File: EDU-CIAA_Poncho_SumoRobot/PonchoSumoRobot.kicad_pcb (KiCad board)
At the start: 2 copper layers, 49 parts, among them K1 RELAY_C, K2 RELAY_C, K3 RELAY_C, K4 RELAY_C, P1 CONN_01X02, P11 CONN_01X02, P12 CONN_01X02, P13 CONN_01X02, P14 CONN_01X02, P15 CONN_01X02, P16 CONN_01X02, P17 CONN_01X02, P18 CONN_01X02, P2 CONN_01X04, P3 CONN_02X09, P4 CONN_01X02, P5 CONN_01X02, P6 CONN_01X04, Q1 BC817-40, Q2 BC817-40, Q3 BC817-40, Q4 BC817-40, U5 40106

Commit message: Reorganizo bibliotecas en esquemático y PCB. Reparo señal de 12V. Agrego Footprints. Coloco plantilla EDU-CIAA. Reparo asociación conector EDU-CIAA en sch y pcb.
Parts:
- removed XA2: Conn_PonchoMP_2x_20x2, Poncho_Esqueleto:Conn_Poncho_Completo
- added G***: LOGO, sumo_robot:Logo_Poncho, F.Cu at (158.8, 137.2)
- added G***: Logo_EDU-CIAA, sumo_robot:Logo_EDU-CIAA, F.Cu at (160.0, 154.9)
- added G101: Logo_OSHWA, sumo_robot:Logo_OSHWA, F.Cu at (158.8, 125.7)
- added MP?: Plantilla_EDU-CIAA, sumo_robot:Plantilla_EDU-CIAA, F.Cu at (119.4, 92.7)
- D1, D2, D3, D4: footprint LEDs:LED_1206 -> sumo_robot:LED_1206
- D5, D6, D7, D8: footprint Diodes_ThroughHole:Diode_DO-41_SOD81_Horizontal_RM10 -> sumo_robot:Diode_DO-41_SOD81_Horizontal_RM10
- K1, K2, K3, K4: footprint Relays_ThroughHole:Relay_SANYOU_SRD_Series_Form_C -> sumo_robot:Relay_SANYOU_SRD_Series_Form_C
- P1, P4, P5: footprint Connect:bornier2 -> sumo_robot:bornier2
- P11, P12, P13, P14, P15, P16, P17, P18: footprint Pin_Headers:Pin_Header_Straight_1x02 -> sumo_robot:Pin_Header_Straight_1x02
- P2, P6: footprint Pin_Headers:Pin_Header_Straight_1x04 -> sumo_robot:Pin_Header_Straight_1x04
- P3: footprint Pin_Headers:Pin_Header_Straight_2x09 -> sumo_robot:Pin_Header_Straight_2x09
- Q1, Q2, Q3, Q4: footprint TO_SOT_Packages_SMD:SOT-23 -> sumo_robot:SOT-23
- R10, R11, R12, R13, R14, R15, R16, R17, R18, R19, R20, R5, R6, R7, R8, R9: footprint Resistors_ThroughHole:Resistor_Horizontal_RM7mm -> sumo_robot:Resistor_Horizontal_RM7mm
- U5: footprint 40xx:40xx-DIL14 -> sumo_robot:40xx-DIL14
- XA1: footprint Poncho_Esqueleto:Conn_Poncho_Completo -> sumo_robot:Conn_Poncho_SinBorde
- moved XA1 126.4 mm to (119.4, 92.7)
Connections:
- K1 pad 3: Net-(K1-Pad3) -> +12V
- K2 pad 3: Net-(K2-Pad3) -> +12V
- K3 pad 3: Net-(K3-Pad3) -> +12V
- K4 pad 3: Net-(K4-Pad3) -> +12V
- P1 pad 1: Net-(P1-Pad1) -> +12V
- P3 pad 18: Net-(P3-Pad18) -> (no net)
- XA1 pad 1: +3V3 -> (no net)
- XA1 pad 20: Net-(XA1-Pad20) -> (no net)
- XA1 pad 22: Net-(XA1-Pad22) -> (no net)
- XA1 pad 24: Net-(XA1-Pad24) -> (no net)
- XA1 pad 26: Net-(XA1-Pad26) -> (no net)
- XA1 pad 28: Net-(XA1-Pad28) -> (no net)
- XA1 pad 30: Net-(XA1-Pad30) -> (no net)
- XA1 pad 32: Net-(XA1-Pad32) -> (no net)
- XA1 pad 33: (no net) -> /UltraSonido/Echo1
- XA1 pad 35: (no net) -> /UltraSonido/Echo2
- XA1 pad 36: (no net) -> /UltraSonido/Triq2
- XA1 pad 37: (no net) -> /UltraSonido/triq1
- XA1 pad 38: Net-(XA1-Pad38) -> (no net)
- XA1 pad 4: Net-(XA1-Pad4) -> (no net)
- XA1 pad 40: Net-(XA1-Pad40) -> (no net)
- XA1 pad 41: Net-(XA1-Pad41) -> (no net)
- XA1 pad 42: +5VP -> (no net)
- XA1 pad 51: Net-(XA1-Pad51) -> (no net)
- XA1 pad 53: Net-(XA1-Pad53) -> (no net)
- XA1 pad 57: Net-(XA1-Pad57) -> (no net)
- XA1 pad 59: Net-(XA1-Pad59) -> (no net)
- XA1 pad 65: Net-(XA1-Pad65) -> (no net)
- XA1 pad 67: Net-(XA1-Pad67) -> (no net)
- XA1 pad 69: (no net) -> Net-(P3-Pad1)
- XA1 pad 71: (no net) -> Net-(P3-Pad5)
- XA1 pad 72: (no net) -> Net-(P3-Pad3)
- XA1 pad 73: (no net) -> Net-(P3-Pad9)
- XA1 pad 74: (no net) -> Net-(P3-Pad7)
- XA1 pad 75: (no net) -> Net-(P3-Pad13)
- XA1 pad 76: (no net) -> Net-(P3-Pad11)
- XA1 pad 78: (no net) -> Net-(P3-Pad15)
- XA1 pad 80: (no net) -> Net-(P3-Pad17)

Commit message: Actualizo trabajo del Poncho Sumo Robot.
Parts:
- removed the G*** at (158.8, 137.2)
- removed the G*** at (160.0, 154.9)
- removed G101: Logo_OSHWA, sumo_robot:Logo_OSHWA
- removed MP?: Plantilla_EDU-CIAA, sumo_robot:Plantilla_EDU-CIAA
- added EESTN2: EESTN2, sumo_robot:LOGO1, F.Cu at (98.0, 134.5)
- added G***: Logo_EDU-CIAA, Poncho_Esqueleto:Logo_EDU-CIAA, F.Cu at (55.9, 35.8)
- added G***: LOGO, sumo_robot:LOGO, F.Cu at (68.2, 96.9)
- added G***: LOGO, sumo_robot:LOGO3, B.Cu at (99.6, 132.5)
- added P7: CONN_01X02, sumo_robot:Pin_Header_Straight_1x02, F.Cu at (58.3, 155.2)
- added P8: CONN_01X02, sumo_robot:Pin_Header_Straight_1x02, F.Cu at (45.5, 151.9)
- added Q5: 2SC1945, Power_Integrations:TO-220, F.Cu at (53.6, 154.4)
- added R1: 470, sumo_robot:Resistor_Horizontal_RM7mm, F.Cu at (51.4, 72.6)
- added R2: 470, sumo_robot:Resistor_Horizontal_RM7mm, F.Cu at (88.4, 72.9)
- added R3: 470, sumo_robot:Resistor_Horizontal_RM7mm, F.Cu at (104.6, 72.6)
- added R4: 470, sumo_robot:Resistor_Horizontal_RM7mm, F.Cu at (69.1, 72.6)
- D1, D2, D3, D4: footprint sumo_robot:LED_1206 -> LEDs:LED-3MM
- Q1, Q2, Q3, Q4: value BC817-40 -> 2SC1945; footprint sumo_robot:SOT-23 -> Power_Integrations:TO-220
- moved P14 51.8 mm to (96.5, 104.0), turned to 0 degrees
- moved P11 49.5 mm to (92.7, 104.0), turned to 0 degrees
- moved P12 47.6 mm to (88.8, 104.0), turned to 0 degrees
- moved Q1 47.3 mm to (55.2, 79.4)
- moved P13 46.2 mm to (84.8, 104.0), turned to 0 degrees
- moved Q2 43.7 mm to (108.7, 79.2)
- moved R12 38.4 mm to (96.6, 92.7), turned to 270 degrees
- moved Q3 35.9 mm to (91.9, 79.5), turned to 0 degrees
- moved R9 35.2 mm to (92.7, 92.8), turned to 270 degrees
- moved R10 32.5 mm to (88.8, 93.0), turned to 270 degrees
- moved R11 30.6 mm to (84.8, 93.0), turned to 270 degrees
- moved R6 19.1 mm to (51.6, 83.8), turned to 0 degrees
- moved R8 16.4 mm to (68.8, 83.8), turned to 0 degrees
- moved R5 15.5 mm to (96.0, 84.1)
- moved R7 14.1 mm to (112.3, 83.8)
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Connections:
- net /UltraSonido/Echo2 renamed Net-(P6-Pad3)
- D1 pad 2: Net-(D1-Pad2) -> +5V
- D2 pad 2: Net-(D2-Pad2) -> +5V
- D3 pad 2: Net-(D3-Pad2) -> +5V
- D4 pad 2: Net-(D4-Pad2) -> +5V
- K1 pad 3: +12V -> Net-(K1-Pad3)
- K2 pad 3: +12V -> Net-(K2-Pad3)
- K3 pad 3: +12V -> Net-(K3-Pad3)
- K4 pad 3: +12V -> Net-(K4-Pad3)
- P1 pad 1: +12V -> Net-(P1-Pad1)
- P2 pad 2: /UltraSonido/triq1 -> Net-(P2-Pad2)
- P2 pad 3: /UltraSonido/Echo1 -> Net-(P2-Pad3)
- P3 pad 18: (no net) -> Net-(P3-Pad18)
- P3 pad 2: Net-(D1-Pad1) -> Net-(P3-Pad2)
- P3 pad 4: Net-(D3-Pad1) -> Net-(P3-Pad4)
- P3 pad 6: Net-(D2-Pad1) -> Net-(P3-Pad6)
- P3 pad 8: Net-(D4-Pad1) -> Net-(P3-Pad8)
- P6 pad 2: /UltraSonido/Triq2 -> Net-(P6-Pad2)
- Q1 pad 3: Net-(D5-Pad2) -> Net-(D6-Pad2)
- Q2 pad 3: Net-(D6-Pad2) -> Net-(D7-Pad2)
- Q3 pad 3: Net-(D7-Pad2) -> Net-(D5-Pad2)
- R5 pad 1: Net-(Q1-Pad1) -> Net-(Q3-Pad1)
- R5 pad 2: Net-(D1-Pad2) -> Net-(P3-Pad2)
- R6 pad 1: Net-(Q2-Pad1) -> Net-(Q1-Pad1)
- R6 pad 2: Net-(D2-Pad2) -> Net-(P3-Pad6)
- R7 pad 1: Net-(Q3-Pad1) -> Net-(Q2-Pad1)
- R7 pad 2: Net-(D3-Pad2) -> Net-(P3-Pad4)
- R8 pad 2: Net-(D4-Pad2) -> Net-(P3-Pad8)
- XA1 pad 1: (no net) -> +3V3
- XA1 pad 20: (no net) -> Net-(XA1-Pad20)
- XA1 pad 22: (no net) -> Net-(XA1-Pad22)
- XA1 pad 24: (no net) -> Net-(XA1-Pad24)
- XA1 pad 26: (no net) -> Net-(XA1-Pad26)
- XA1 pad 28: (no net) -> Net-(XA1-Pad28)
- XA1 pad 30: (no net) -> Net-(XA1-Pad30)
- XA1 pad 31: (no net) -> Net-(XA1-Pad31)
- XA1 pad 32: (no net) -> Net-(XA1-Pad32)
- XA1 pad 33: /UltraSonido/Echo1 -> Net-(P2-Pad2)
- XA1 pad 34: (no net) -> Net-(XA1-Pad34)
- XA1 pad 36: /UltraSonido/Triq2 -> Net-(P2-Pad3)
- XA1 pad 37: /UltraSonido/triq1 -> Net-(P6-Pad2)
- XA1 pad 38: (no net) -> Net-(XA1-Pad38)
- XA1 pad 39: (no net) -> Net-(XA1-Pad39)
- XA1 pad 4: (no net) -> Net-(XA1-Pad4)
- XA1 pad 40: (no net) -> Net-(XA1-Pad40)
- XA1 pad 41: (no net) -> Net-(XA1-Pad41)
- XA1 pad 42: (no net) -> +5VP
- XA1 pad 51: (no net) -> Net-(XA1-Pad51)
- XA1 pad 53: (no net) -> Net-(XA1-Pad53)
- XA1 pad 57: (no net) -> Net-(XA1-Pad57)
- XA1 pad 59: (no net) -> Net-(XA1-Pad59)
- XA1 pad 65: (no net) -> Net-(XA1-Pad65)
- XA1 pad 67: (no net) -> Net-(XA1-Pad67)
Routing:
- net GND: track 164.1 -> 439.5 mm, vias 8 -> 11
- net +5V: track 183.6 -> 345.8 mm, vias 0 -> 2
- net Net-(P3-Pad5): track 0.00 -> 93.7 mm, vias 0 -> 2
- net Net-(K1-Pad3): track 0.00 -> 89.0 mm
- net Net-(P3-Pad1): track 0.00 -> 84.7 mm
- net Net-(D3-Pad1): track 73.4 -> 7.28 mm, vias 1 -> 0
- net Net-(P3-Pad4): track 0.00 -> 61.9 mm
- net Net-(D1-Pad1): track 56.8 -> 7.39 mm, vias 1 -> 0
- net Net-(D2-Pad1): track 57.0 -> 7.72 mm, vias 1 -> 0
- net Net-(P3-Pad9): track 0.00 -> 48.0 mm, vias 0 -> 4
- net Net-(D4-Pad1): track 53.3 -> 7.52 mm, vias 1 -> 0
- net Net-(P3-Pad2): track 0.00 -> 43.6 mm
- net Net-(P3-Pad6): track 0.00 -> 42.8 mm, vias 0 -> 2
- net Net-(P3-Pad8): track 0.00 -> 42.6 mm, vias 0 -> 2
- net Net-(P3-Pad18): track 0.00 -> 25.1 mm
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- added copper zone on B.Cu, net GND
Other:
- board outline added: 85.9 x 137.2 mm
- net class Default: clearance 0.3048 -> 0.5
- rule trace_clearance: 0.3048 -> 0.5
- board text added: "PONCHO SUMO ROBOT"

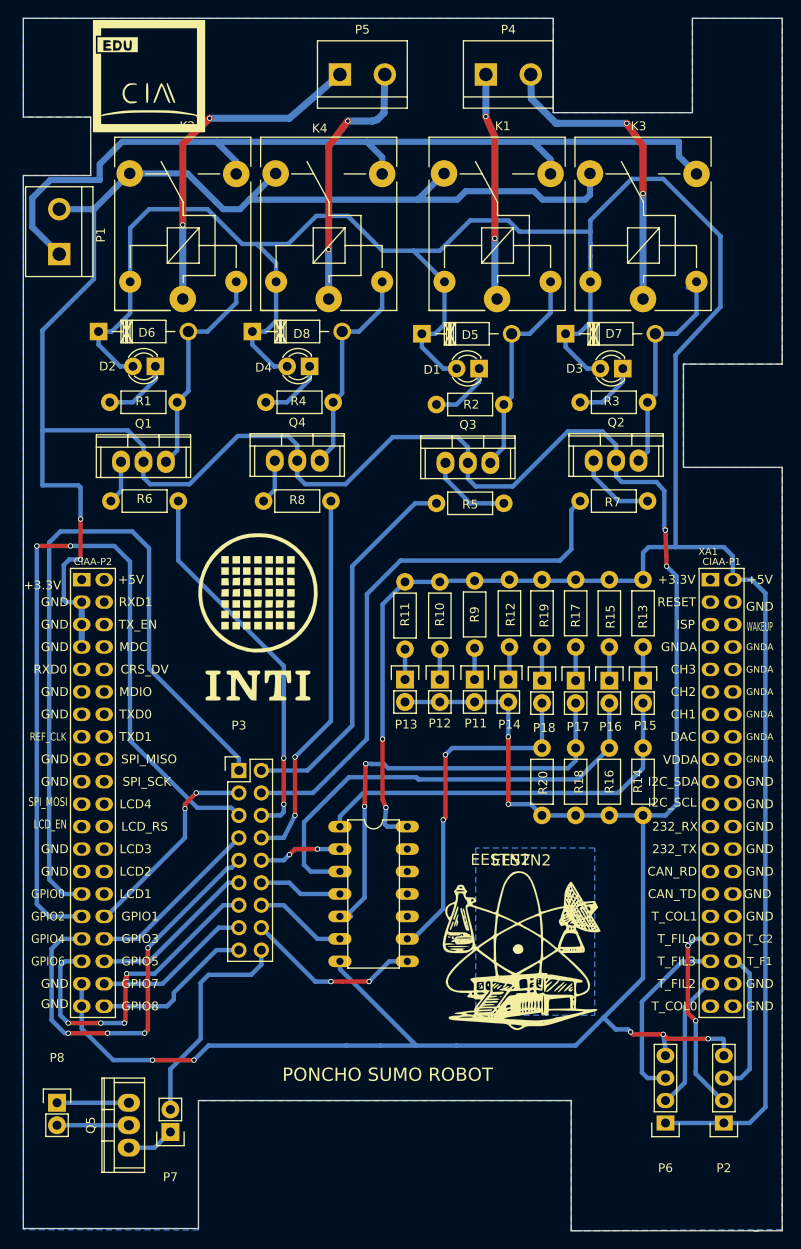
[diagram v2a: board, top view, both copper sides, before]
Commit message: EDU-CIAA Poncho Sumo Robot. Ultimos cambios de vías y puentes para simple faz.
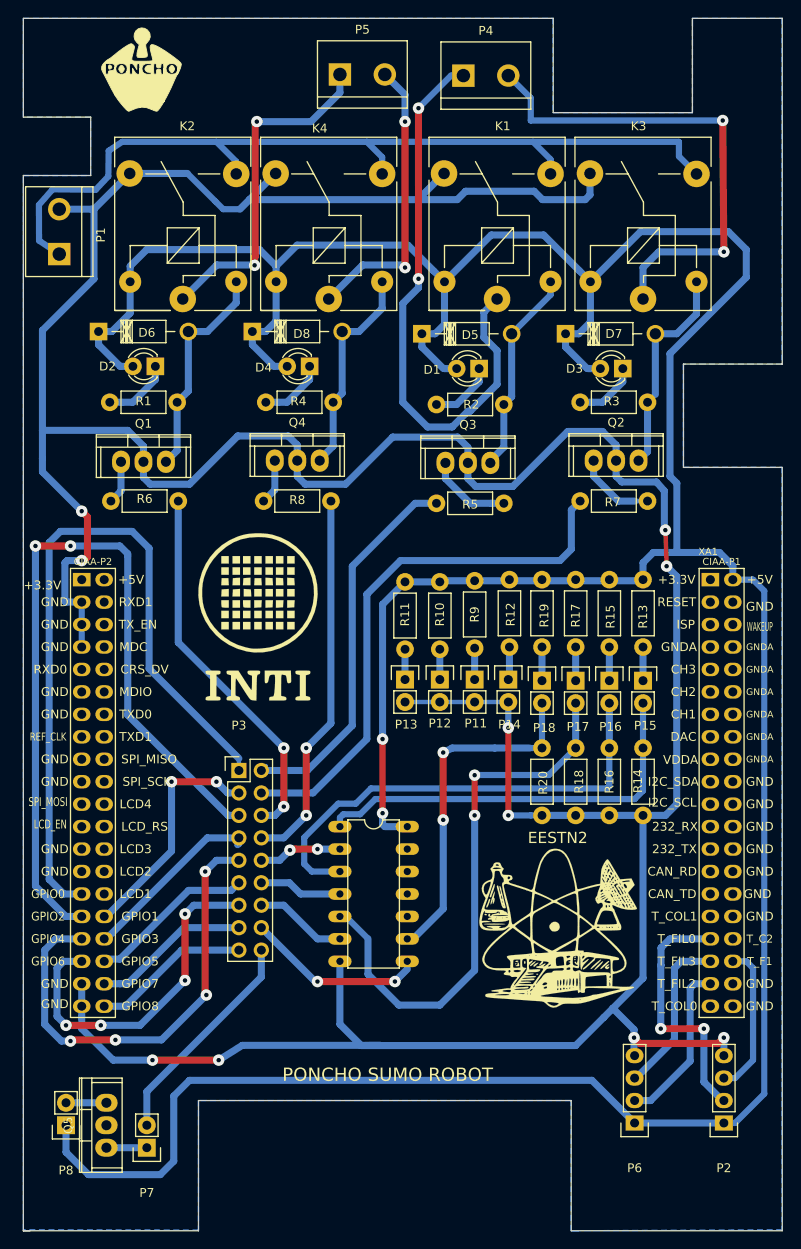
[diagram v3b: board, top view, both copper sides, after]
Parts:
- removed the G*** at (55.9, 35.8)
- removed the G*** at (99.6, 132.5)
- added G***: LOGO, sumo_robot:Logo_Poncho, F.Cu at (55.0, 35.1)
- moved EESTN2 4.85 mm to (102.1, 132.0)
- moved P6 3.49 mm to (110.8, 154.2)
- moved P7 3.21 mm to (55.6, 157.0)
- moved P8 2.74 mm to (46.5, 154.4), turned to 180 degrees
- moved P4 2.54 mm to (94.0, 35.7)
- moved Q5 2.54 mm to (51.1, 154.4)
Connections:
- K1 pad 3: Net-(K1-Pad3) -> +12V
- K2 pad 3: Net-(K2-Pad3) -> +12V
- K3 pad 3: Net-(K3-Pad3) -> +12V
- K4 pad 3: Net-(K4-Pad3) -> +12V
- P1 pad 1: Net-(P1-Pad1) -> +12V
- P8 pad 1: Net-(P8-Pad1) -> +5V
- Q5 pad 2: Net-(P8-Pad2) -> Net-(Q5-Pad2)
- Q5 pad 3: Net-(P8-Pad1) -> Net-(P8-Pad2)
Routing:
- net +12V: track 0.00 -> 101.9 mm
- net Net-(K1-Pad3): track 89.0 -> 0.00 mm
- net +5V: track 345.8 -> 409.8 mm
- net Net-(K1-Pad1): track 25.7 -> 65.7 mm
- net Net-(K3-Pad1): track 35.1 -> 56.1 mm
- net Net-(P17-Pad2): track 50.9 -> 63.2 mm
- net Net-(P8-Pad1): track 8.13 -> 0.00 mm
- net Net-(P2-Pad2): track 22.8 -> 29.8 mm
- net Net-(P3-Pad9): track 48.0 -> 53.4 mm
- net Net-(K2-Pad3): track 4.56 -> 0.00 mm
- net Net-(P1-Pad1): track 4.31 -> 0.00 mm
- net Net-(P6-Pad2): track 15.5 -> 19.1 mm
- net Net-(P8-Pad2): track 8.13 -> 4.57 mm
- net Net-(K4-Pad1): track 29.6 -> 33.1 mm
- net Net-(P3-Pad3): track 23.2 -> 26.7 mm
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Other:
- outline, holes or cut-outs redrawn
- net class Default: clearance 0.5 -> 0.25; trace_width 0.25 -> 0.5
- rule trace_clearance: 0.5 -> 0.25

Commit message: Anoto correcciones al Poncho Sumo.
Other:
- board text added: "*cambiar a TO92. *Falta una conexión. *Referencias debajo de componentes. * Modelos 3D."
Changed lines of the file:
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@@
-(kicad_pcb (version 4) (host pcbnew 4.0.3+e1-6302~38~ubuntu14.04.1-stable)
+(kicad_pcb (version 4) (host pcbnew 4.0.2+dfsg1-2~bpo8+1-stable)
   (general
     (links 116)
     (no_connects 1)
-    (area 41.398667 29.134999 127.583001 166.445001)
+    (area 41.580999 29.134999 127.583001 166.445001)
     (thickness 1.6)
-    (drawings 22)
+    (drawings 23)
     (tracks 566)
     (zones 0)
@@
   (page A4)
   (layers
-    (0 F.Cu signal hide)
-    (31 B.Cu signal hide)
+    (0 F.Cu signal)
+    (31 B.Cu signal)
     (32 B.Adhes user hide)
     (33 F.Adhes user hide)
@@
     (38 B.Mask user hide)
     (39 F.Mask user hide)
-    (40 Dwgs.User user hide)
+    (40 Dwgs.User user)
     (41 Cmts.User user hide)
     (42 Eco1.User user hide)
@@
     (pad_to_mask_clearance 0.2)
     (aux_axis_origin 46.355 161.544)
-    (visible_elements 7FFC7D1F)
+    (visible_elements 7FFEFD3F)
     (pcbplotparams
       (layerselection 0x01020_80000000)
@@
       (xy 3.778435 -0.1467) (xy 3.778435 -0.1467)) (layer F.SilkS) (width 0.1))
   )
+  (gr_text "*cambiar a TO92.\n*Falta una conexión.\n*Referencias debajo de componentes.\n* Modelos 3D.\n" (at 130 95) (layer Dwgs.User)
+    (effects (font (size 1.5 1.5) (thickness 0.3)) (justify left))
+  )
   (gr_line (start 41.656 166.37) (end 42.418 166.37) (angle 90) (layer Edge.Cuts) (width 0.15))
